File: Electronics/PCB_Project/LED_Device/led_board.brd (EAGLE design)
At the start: 100 x 80 mm, 12 parts, among them CN1 9V, IC1 7805DT, SW1 push

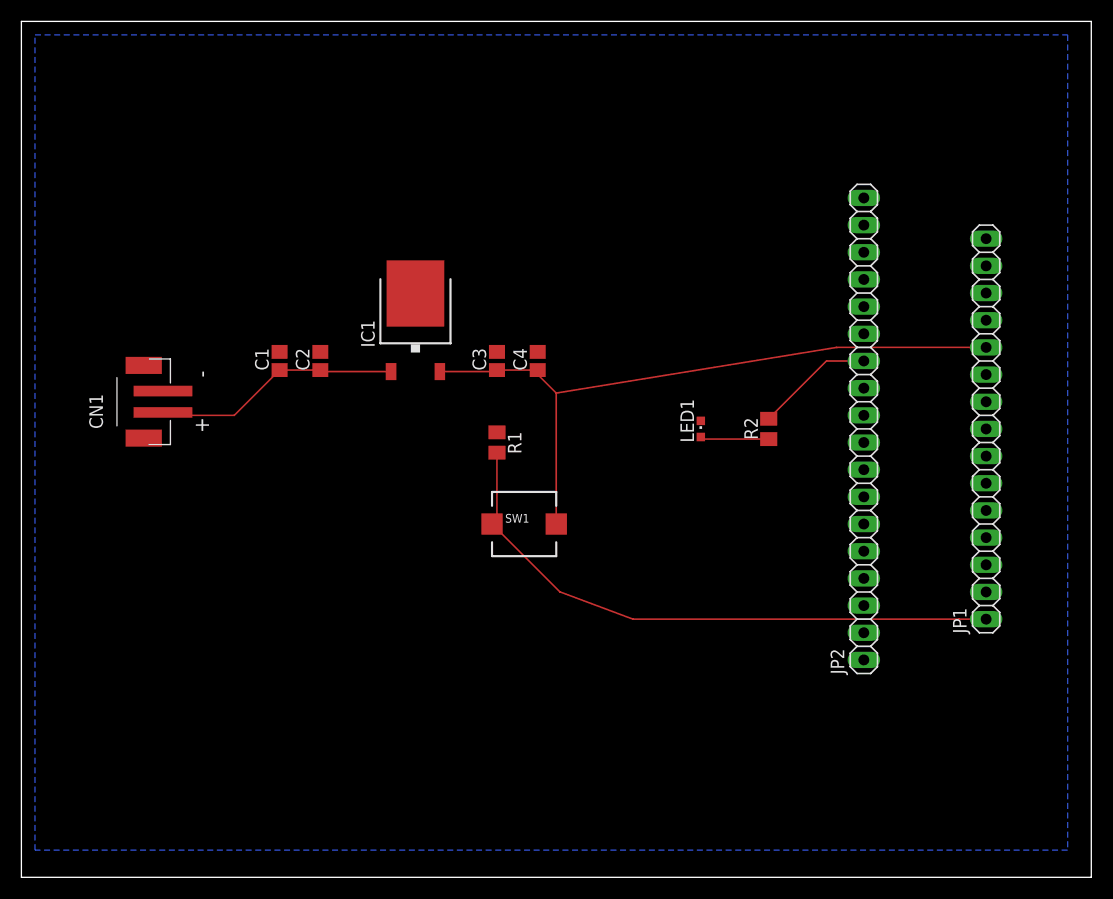
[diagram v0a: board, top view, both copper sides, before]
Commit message: added working ground plane
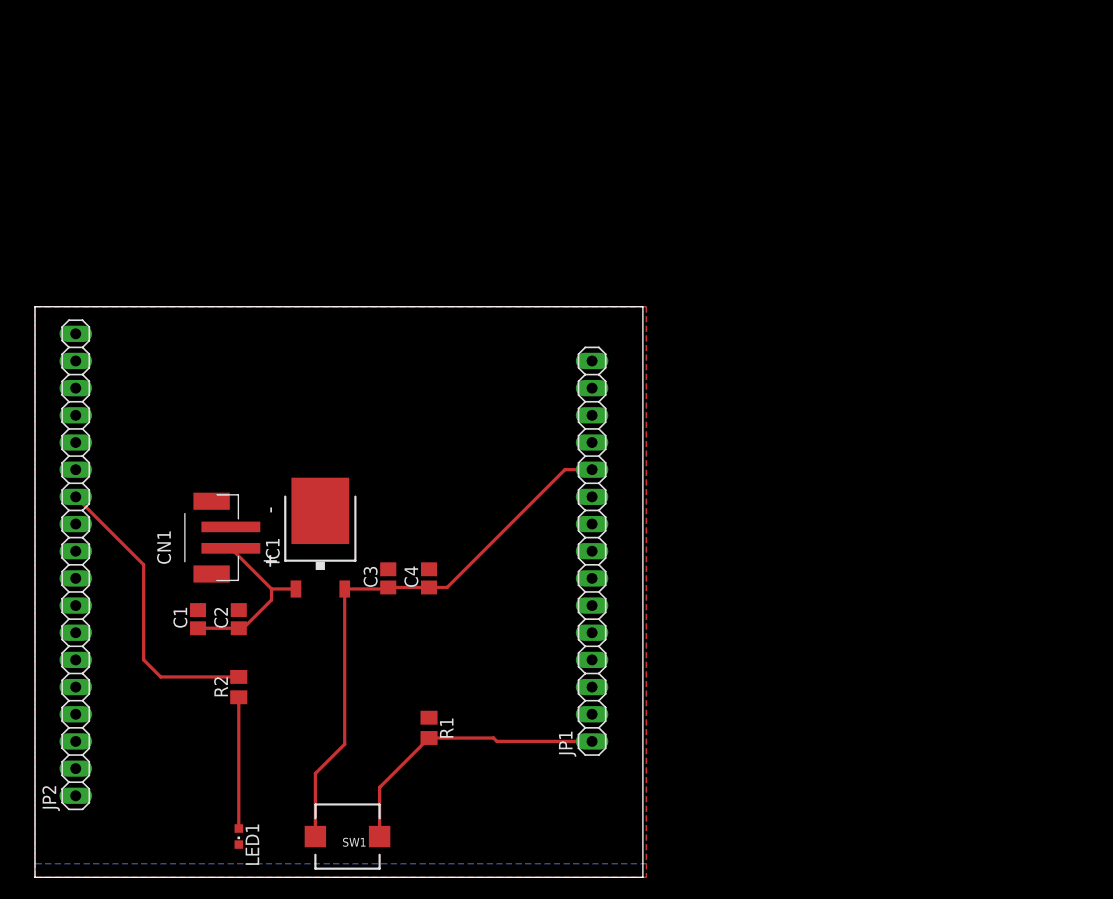
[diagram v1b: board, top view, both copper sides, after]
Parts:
- moved JP2 74.7 mm to (5.08, 29.2)
- moved LED1 57.6 mm to (20.3, 3.81), turned to 180 degrees
- moved R2 55.1 mm to (20.3, 17.8)
- moved JP1 38.6 mm to (53.3, 30.5)
- moved SW1 33.6 mm to (30.5, 3.81), turned to 180 degrees
- moved R1 27.4 mm to (38.1, 14.0)
- moved C1 25.3 mm to (16.5, 24.1)
- moved C2 25.3 mm to (20.3, 24.1)
- moved C3 22.7 mm to (34.3, 27.9)
- moved C4 22.7 mm to (38.1, 27.9)
- moved IC1 22.2 mm to (27.9, 31.8)
- moved CN1 14.2 mm to (17.8, 31.8)
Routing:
- net BUTTON: track 55.9 -> 26.5 mm
- net N$7: track 11.1 -> 27.4 mm
- net 5V: track 64.4 -> 52.0 mm
- net N$3: track 6.43 -> 12.3 mm
- net N$1: track 21.1 -> 17.2 mm
- net GRND: track 3.39 -> 0.00 mm
- added copper zone on layer 1, net GRND
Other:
- board size 100 x 80 mm -> 56.8 x 53.3 mm

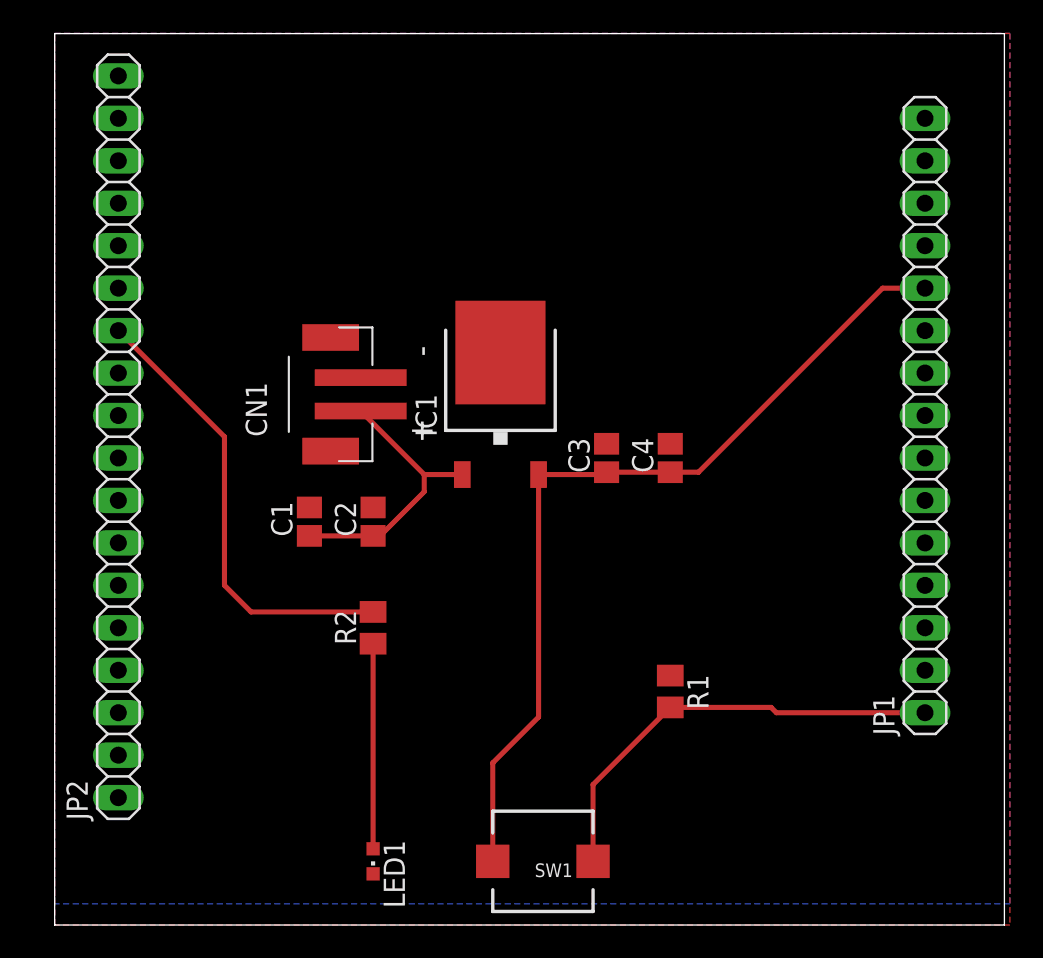
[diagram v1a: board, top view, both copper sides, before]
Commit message: changed PCB design to have ATMEGA328 and crystal
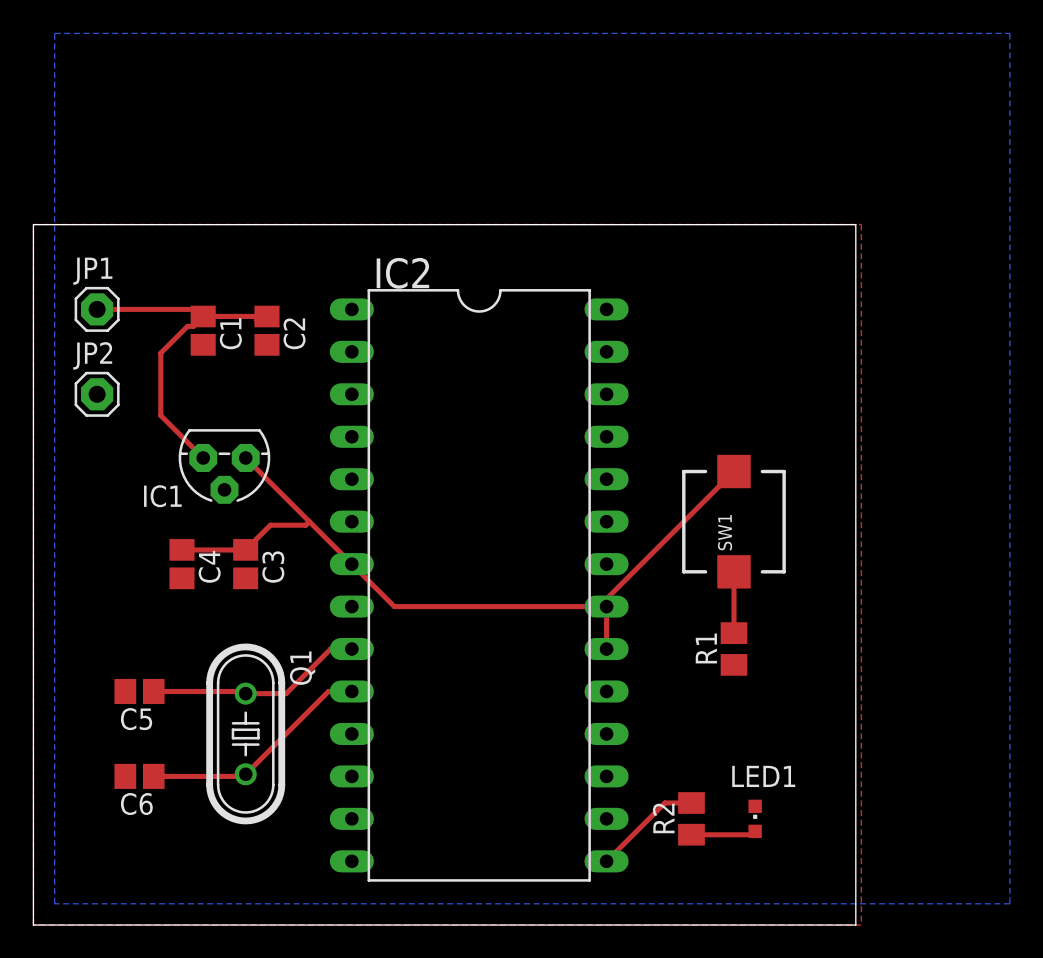
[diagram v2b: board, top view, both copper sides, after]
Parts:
- removed CN1: 9V, adafruit:JST-PH-2-SMT
- added C5, C6: 10u, adafruit:C0805
- added IC2: (no value), ic-package:DIL28-6
- added Q1: (no value), adafruit:HC49/S
- IC1: value 7805DT -> 7805L; device adafruit:TO252 -> adafruit:TO92
- JP1: value header1 -> (none); device adafruit:1X15 -> adafruit:1X01
- JP2: value header2 -> (none); device adafruit:1X18 -> adafruit:1X01
- moved JP1 49.9 mm to (3.81, 36.8), turned to 0 degrees
- moved C4 29.9 mm to (8.89, 21.6), turned to 270 degrees
- moved SW1 23.3 mm to (41.9, 24.1), turned to 90 degrees
- moved LED1 23.0 mm to (43.2, 6.35), turned to 0 degrees
- moved C3 22.5 mm to (12.7, 21.6), turned to 270 degrees
- moved R2 22.2 mm to (39.4, 6.35)
- moved IC1 16.9 mm to (11.4, 27.9), turned to 180 degrees
- moved C1 13.1 mm to (10.2, 35.6), turned to 270 degrees
- moved C2 13.1 mm to (14.0, 35.6), turned to 270 degrees
- moved R1 4.58 mm to (41.9, 16.5), turned to 90 degrees
- moved JP2 2.84 mm to (3.81, 31.8), turned to 0 degrees
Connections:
- new net N$2: IC2.22
- new net N$4: C5.1, IC2.9, Q1.1
- new net N$5: C6.1, IC2.10, Q1.2
- net 5V: now also IC1.1, IC2.20, IC2.21, IC2.7; no longer IC1.2, JP1.11
- net BUTTON: no longer JP1.1
- net GRND: now also C5.2, C6.2, IC1.2, JP2.1; no longer CN1.2, IC1.3, JP2.15
- net N$1: now also IC1.3, JP1.1; no longer CN1.1, IC1.1
- net N$7: now also IC2.15; no longer JP2.12
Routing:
- net BUTTON: track 26.5 -> 3.67 mm
- net N$7: track 27.4 -> 6.53 mm
- net N$5: track 0.00 -> 14.0 mm
- net N$4: track 0.00 -> 13.0 mm
- net N$3: track 12.3 -> 4.29 mm
- net 5V: track 52.0 -> 47.6 mm
- net N$1: track 17.2 -> 21.6 mm
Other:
- board size 56.8 x 53.3 mm -> 49.2 x 41.9 mm
